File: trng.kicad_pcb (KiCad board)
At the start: 2 copper layers, 21.8 x 16.3 mm, 22 parts, among them J1 USB_A, U1 FT240XQ, U2 MC74VHC1G66DFT1G, U3 MC74VHC1G66DFT1G, U4 TSV912IQ2T, U5 TS3022IYST

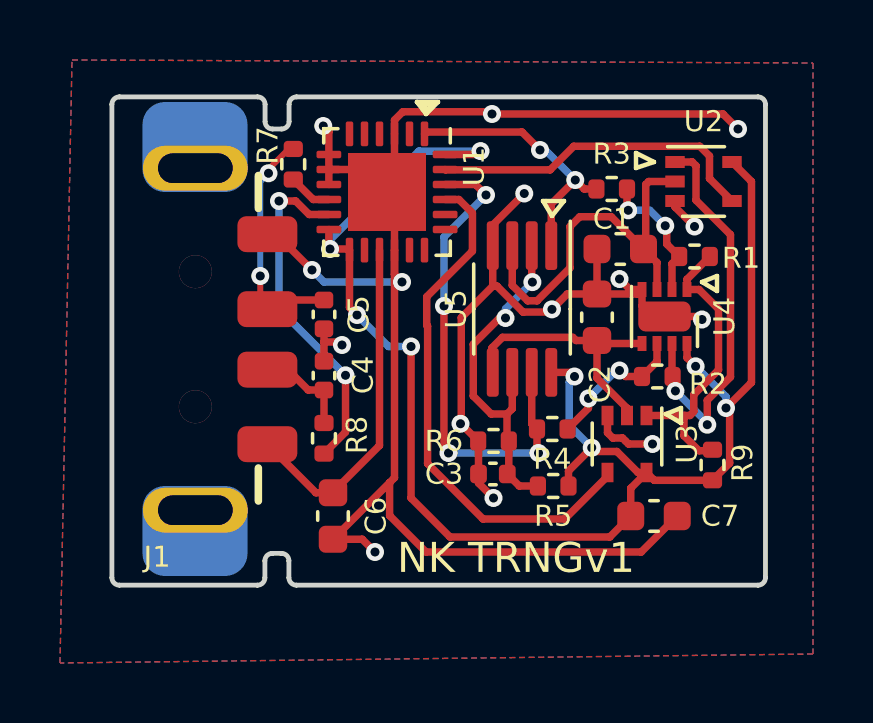
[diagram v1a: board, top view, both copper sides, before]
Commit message: Add test header and recreate production data
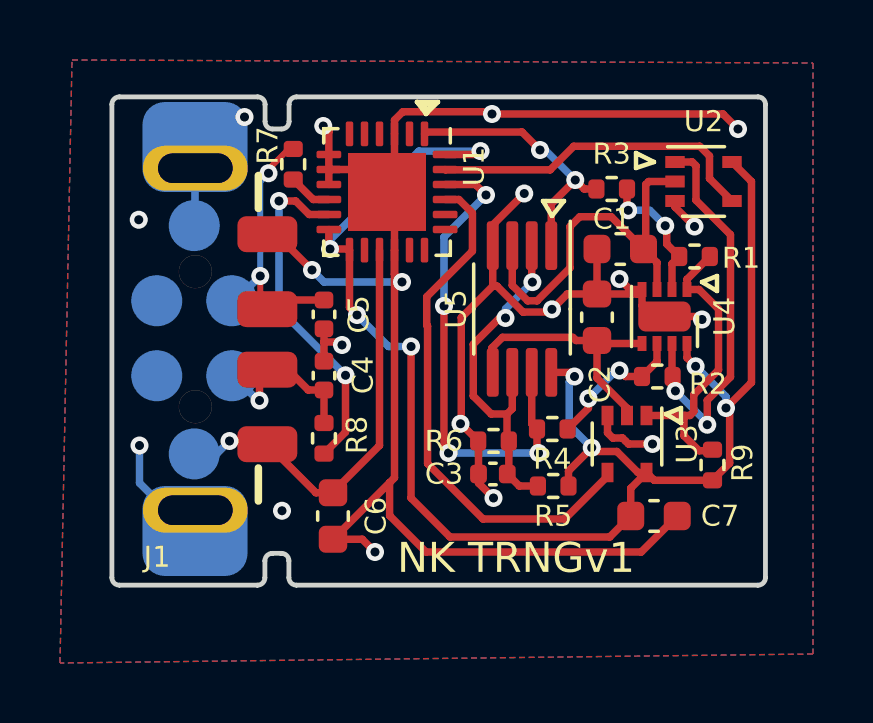
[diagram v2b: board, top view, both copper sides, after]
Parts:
- added J2: Conn_01x06, cl6:nitro_programming_header, B.Cu at (136.1, 77.7)
- J1: value USB_A -> 0480372200
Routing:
- net GND: track 78.0 -> 83.4 mm, vias 15 -> 19
- net /VBUS: track 11.6 -> 14.2 mm, vias 0 -> 1
- net /D-: track 3.27 -> 5.66 mm, vias 0 -> 1
- net /D+: track 7.95 -> 9.21 mm
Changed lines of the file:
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@@
   (net 26 "/VBUS")
   (net 27 "unconnected-(U1-Pad14)")
+  (net 28 "unconnected-(J2-Pad5)")
+  (net 29 "unconnected-(J2-Pad6)")
   (footprint "Capacitor_SMD:C_0603_1608Metric" (layer "F.Cu")
     (at 151.4 83.6)
@@
       (effects (font (size 0.7 0.7) (thickness 0.25)))
     )
-    (fp_text value "USB_A" (at 1 -9) (layer "B.SilkS") hide
+    (fp_text value "0480372200" (at 1 -9) (layer "B.SilkS") hide
       (effects (font (size 1.524 1.524) (thickness 0.3048)) (justify mirror))
     )
@@
       (rotate (xyz 0 0 0))
     )
+  )
+  (footprint "cl6:nitro_programming_header" (layer "B.Cu")
+    (at 136.075 77.675 180)
+    (property "Sheetfile" "trng.kicad_sch")
+    (property "Sheetname" "")
+    (attr smd)
+    (fp_text reference "J2" (at 3.6 -1.22) (layer "B.SilkS") hide
+      (effects (font (size 1 1) (thickness 0.15)) (justify mirror))
+    )
+    (fp_text value "Conn_01x06" (at 5.3742 -0.355 90) (layer "B.Fab") hide
+      (effects (font (size 1 1) (thickness 0.15)) (justify mirror))
+    )
+    (pad "1" smd circle (at 0 3.755 180) (size 1.7 1.7) (layers "B.Cu" "B.Mask")
+      (net 2 "GND") (pinfunction "Pin_1") (pintype "passive"))
+    (pad "2" smd circle (at -1.25 1.25 180) (size 1.7 1.7) (layers "B.Cu" "B.Mask")
+      (net 23 "/D+") (pinfunction "Pin_2") (pintype "passive"))
+    (pad "3" smd circle (at -1.25 -1.25 180) (size 1.7 1.7) (layers "B.Cu" "B.Mask")
+      (net 22 "/D-") (pinfunction "Pin_3") (pintype "passive"))
+    (pad "4" smd circle (at 0 -3.855 180) (size 1.7 1.7) (layers "B.Cu" "B.Mask")
+      (net 26 "/VBUS") (pinfunction "Pin_4") (pintype "passive"))
+    (pad "5" smd circle (at 1.25 1.25 180) (size 1.7 1.7) (layers "B.Cu" "B.Mask")
+      (net 28 "unconnected-(J2-Pad5)") (pinfunction "Pin_5") (pintype "passive+no_connect"))
+    (pad "6" smd circle (at 1.25 -1.25 180) (size 1.7 1.7) (layers "B.Cu" "B.Mask")
+      (net 29 "unconnected-(J2-Pad6)") (pinfunction "Pin_6") (pintype "passive+no_connect"))
   )
   (gr_line (start 143.5 69.8) (end 144 69.9) (layer "F.SilkS") (width 0.15))
@@
   (segment (start 150.975 84.8) (end 143.8 84.8) (width 0.25) (layer "F.Cu") (net 2))
   (via (at 147.075 72.85) (size 0.6) (drill 0.3) (layers "F.Cu" "B.Cu") (net 2))
+  (via (at 139 83.425) (size 0.6) (drill 0.3) (layers "F.Cu" "B.Cu") (free) (net 2))
   (via (at 152.75 73.95) (size 0.6) (drill 0.3) (layers "F.Cu" "B.Cu") (net 2))
   (via (at 143 75.8) (size 0.6) (drill 0.3) (layers "F.Cu" "B.Cu") (net 2))
@@
   (via (at 146 70.2) (size 0.6) (drill 0.3) (layers "F.Cu" "B.Cu") (net 2))
   (via (at 140 75.4) (size 0.6) (drill 0.3) (layers "F.Cu" "B.Cu") (net 2))
+  (via (at 134.25 81.25) (size 0.6) (drill 0.3) (layers "F.Cu" "B.Cu") (free) (net 2))
+  (via (at 134.225 73.725) (size 0.6) (drill 0.3) (layers "F.Cu" "B.Cu") (free) (net 2))
   (via (at 140.375 70.6) (size 0.6) (drill 0.3) (layers "F.Cu" "B.Cu") (net 2))
   (via (at 142.1 84.8) (size 0.6) (drill 0.3) (layers "F.Cu" "B.Cu") (net 2))
+  (via (at 137.75 70.3) (size 0.6) (drill 0.3) (layers "F.Cu" "B.Cu") (net 2))
   (via (at 141 77.9) (size 0.6) (drill 0.3) (layers "F.Cu" "B.Cu") (net 2))
   (via (at 150.25 75.7) (size 0.6) (drill 0.3) (layers "F.Cu" "B.Cu") (net 2))
@@
   (via (at 147.998703 76.711177) (size 0.6) (drill 0.3) (layers "F.Cu" "B.Cu") (net 2))
   (via (at 146.05 83) (size 0.6) (drill 0.3) (layers "F.Cu" "B.Cu") (net 2))
+  (segment (start 136.1 72.01846) (end 136.11182 72.00664) (width 0.25) (layer "B.Cu") (net 2))
+  (segment (start 136.1 73.895) (end 136.1 72.01846) (width 0.25) (layer "B.Cu") (net 2))
   (segment (start 140.4 75.8) (end 143 75.8) (width 0.25) (layer "B.Cu") (net 2))
+  (segment (start 134.25 81.25) (end 134.25 82.5) (width 0.25) (layer "B.Cu") (net 2))
+  (segment (start 134.25 82.5) (end 135.15616 83.40616) (width 0.25) (layer "B.Cu") (net 2))
   (segment (start 140 75.4) (end 140.4 75.8) (width 0.25) (layer "B.Cu") (net 2))
+  (segment (start 135.15616 83.40616) (end 136.11182 83.40616) (width 0.25) (layer "B.Cu") (net 2))
   (segment (start 149.5 79.004941) (end 149.5 77.75) (width 0.25) (layer "F.Cu") (net 3))
   (segment (start 150.5 80.004941) (end 149.5 79.004941) (width 0.25) (layer "F.Cu") (net 3))
@@
   (segment (start 148.724511 71.275489) (end 152.925489 71.275489) (width 0.25) (layer "F.Cu") (net 21))
   (segment (start 152.925489 71.275489) (end 153.25 71.6) (width 0.25) (layer "F.Cu") (net 21))
+  (segment (start 138.25 78.9848) (end 138.25 79.75) (width 0.25) (layer "F.Cu") (net 22))
   (segment (start 139.875 79.4) (end 139.1974 78.7224) (width 0.25) (layer "F.Cu") (net 22))
+  (segment (start 138.5124 78.7224) (end 138.25 78.9848) (width 0.25) (layer "F.Cu") (net 22))
   (segment (start 139.1974 78.7224) (end 138.5124 78.7224) (width 0.25) (layer "F.Cu") (net 22))
   (segment (start 140.4 80.5) (end 140.4 79.4) (width 0.25) (layer "F.Cu") (net 22))
   (segment (start 140.4 79.4) (end 139.875 79.4) (width 0.25) (layer "F.Cu") (net 22))
+  (via (at 138.25 79.75) (size 0.6) (drill 0.3) (layers "F.Cu" "B.Cu") (net 22))
+  (segment (start 137.35 78.9) (end 138.2 79.75) (width 0.25) (layer "B.Cu") (net 22))
+  (segment (start 138.2 79.75) (end 138.25 79.75) (width 0.25) (layer "B.Cu") (net 22))
   (segment (start 138.2755 76.46874) (end 138.2755 75.6) (width 0.2) (layer "F.Cu") (net 23))
   (segment (start 138.81804 76.4) (end 138.5124 76.70564) (width 0.25) (layer "F.Cu") (net 23))
@@
   (via (at 138.55 72.175) (size 0.6) (drill 0.3) (layers "F.Cu" "B.Cu") (net 23))
   (via (at 138.2755 75.6) (size 0.6) (drill 0.3) (layers "F.Cu" "B.Cu") (net 23))
+  (segment (start 137.35 76.4) (end 137.4755 76.4) (width 0.25) (layer "B.Cu") (net 23))
   (segment (start 138.2755 75.6) (end 138.2755 72.4495) (width 0.2) (layer "B.Cu") (net 23))
   (segment (start 138.2755 72.4495) (end 138.55 72.175) (width 0.2) (layer "B.Cu") (net 23))
+  (segment (start 137.4755 76.4) (end 138.2755 75.6) (width 0.25) (layer "B.Cu") (net 23))
   (segment (start 140.5625 73.05) (end 140.04 73.05) (width 0.25) (layer "F.Cu") (net 24))
   (segment (start 140.04 73.05) (end 139.3 72.31) (width 0.25) (layer "F.Cu") (net 24))
@@
   (segment (start 142.25 81.25) (end 142.25 74.7375) (width 0.25) (layer "F.Cu") (net 26))
   (segment (start 140.13088 82.825) (end 138.5124 81.20652) (width 0.25) (layer "F.Cu") (net 26))
+  (segment (start 137.25 81.1) (end 138.40588 81.1) (width 0.25) (layer "F.Cu") (net 26))
   (segment (start 140.7 82.8) (end 142.25 81.25) (width 0.25) (layer "F.Cu") (net 26))
   (segment (start 140.7 82.825) (end 140.7 82.8) (width 0.25) (layer "F.Cu") (net 26))
+  (segment (start 138.40588 81.1) (end 138.5124 81.20652) (width 0.25) (layer "F.Cu") (net 26))
+  (via (at 137.25 81.1) (size 0.6) (drill 0.3) (layers "F.Cu" "B.Cu") (net 26))
+  (segment (start 136.845 81.505) (end 137.25 81.1) (width 0.25) (layer "B.Cu") (net 26))
+  (segment (start 136.1 81.505) (end 136.845 81.505) (width 0.25) (layer "B.Cu") (net 26))
   (zone (net 2) (net_name "GND") (layers F&B.Cu) (hatch edge 0.508)
     (connect_pads (clearance 0.308))
